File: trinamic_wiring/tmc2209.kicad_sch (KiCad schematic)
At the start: 0 parts

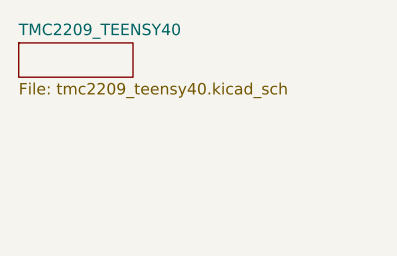
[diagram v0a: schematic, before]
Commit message: Add tmc2209_mega2560
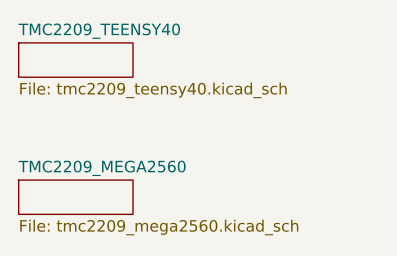
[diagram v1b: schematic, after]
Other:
- added sheet TMC2209_MEGA2560 (tmc2209_mega2560.kicad_sch)
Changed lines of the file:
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@@
+    )
+  )
+  (sheet (at 100.33 50.8) (size 12.7 3.81) (fields_autoplaced)
+    (stroke (width 0.1524) (type solid) (color 0 0 0 0))
+    (fill (color 0 0 0 0.0000))
+    (property "Sheet name" "TMC2209_MEGA2560" (id 0) (at 100.33 50.0884 0)
+      (effects (font (size 1.27 1.27)) (justify left bottom))
+    )
+    (property "Sheet file" "tmc2209_mega2560.kicad_sch" (id 1) (at 100.33 55.1946 0)
+      (effects (font (size 1.27 1.27)) (justify left top))
     )
   )

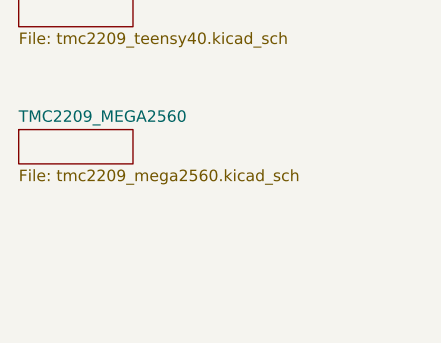
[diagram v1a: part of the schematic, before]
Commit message: Add tmc2209_feather_nrf52
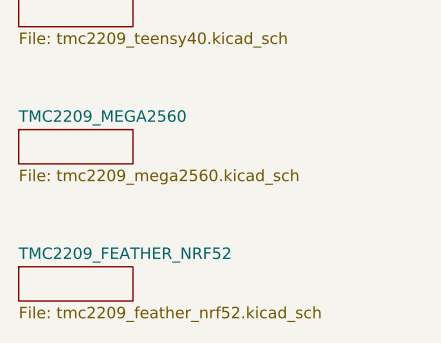
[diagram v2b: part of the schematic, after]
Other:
- added sheet TMC2209_FEATHER_NRF52 (tmc2209_feather_nrf52.kicad_sch)
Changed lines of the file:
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@@
+    )
+  )
+  (sheet (at 100.33 66.04) (size 12.7 3.81) (fields_autoplaced)
+    (stroke (width 0.1524) (type solid) (color 0 0 0 0))
+    (fill (color 0 0 0 0.0000))
+    (property "Sheet name" "TMC2209_FEATHER_NRF52" (id 0) (at 100.33 65.3284 0)
+      (effects (font (size 1.27 1.27)) (justify left bottom))
+    )
+    (property "Sheet file" "tmc2209_feather_nrf52.kicad_sch" (id 1) (at 100.33 70.4346 0)
+      (effects (font (size 1.27 1.27)) (justify left top))
     )
   )

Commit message: Update version
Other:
- company: (none) -> Janelia Research Campus
- title: (none) -> Trinamic Wiring
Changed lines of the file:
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@@
-(kicad_sch (version 20211123) (generator eeschema)
+(kicad_sch (version 20230121) (generator eeschema)
   (paper "A4")
+  (title_block
+    (title "Trinamic Wiring")
+    (date "2023-04-18")
+    (rev "0.3")
+    (company "Janelia Research Campus")
+  )
   (sheet (at 100.33 35.56) (size 12.7 3.81) (fields_autoplaced)
-    (stroke (width 0.1524) (type solid) (color 0 0 0 0))
+    (stroke (width 0.1524) (type solid))
     (fill (color 0 0 0 0.0000))
-    (property "Sheet name" "TMC2209_TEENSY40" (id 0) (at 100.33 34.8484 0)
+    (property "Sheetname" "TMC2209_TEENSY40" (at 100.33 34.8484 0)
       (effects (font (size 1.27 1.27)) (justify left bottom))
     )
-    (property "Sheet file" "tmc2209_teensy40.kicad_sch" (id 1) (at 100.33 39.9546 0)
+    (property "Sheetfile" "tmc2209_teensy40.kicad_sch" (at 100.33 39.9546 0)
       (effects (font (size 1.27 1.27)) (justify left top))
+    )
+    (instances
+      (project "trinamic_wiring"
+        (path "/e4144788-6304-493f-818e-5d881d3b7418/c8eda2b5-ab13-4033-82d9-875c9fcaf884" (page "3"))
+      )
     )
   )
   (sheet (at 100.33 66.04) (size 12.7 3.81) (fields_autoplaced)
-    (stroke (width 0.1524) (type solid) (color 0 0 0 0))
+    (stroke (width 0.1524) (type solid))
     (fill (color 0 0 0 0.0000))
-    (property "Sheet name" "TMC2209_FEATHER_NRF52" (id 0) (at 100.33 65.3284 0)
+    (property "Sheetname" "TMC2209_FEATHER_NRF52" (at 100.33 65.3284 0)
       (effects (font (size 1.27 1.27)) (justify left bottom))
     )
-    (property "Sheet file" "tmc2209_feather_nrf52.kicad_sch" (id 1) (at 100.33 70.4346 0)
+    (property "Sheetfile" "tmc2209_feather_nrf52.kicad_sch" (at 100.33 70.4346 0)
       (effects (font (size 1.27 1.27)) (justify left top))
+    )
+    (instances
+      (project "trinamic_wiring"
+        (path "/e4144788-6304-493f-818e-5d881d3b7418/c8eda2b5-ab13-4033-82d9-875c9fcaf884" (page "5"))
+      )
     )
   )
   (sheet (at 100.33 50.8) (size 12.7 3.81) (fields_autoplaced)
-    (stroke (width 0.1524) (type solid) (color 0 0 0 0))
+    (stroke (width 0.1524) (type solid))
     (fill (color 0 0 0 0.0000))
-    (property "Sheet name" "TMC2209_MEGA2560" (id 0) (at 100.33 50.0884 0)
+    (property "Sheetname" "TMC2209_MEGA2560" (at 100.33 50.0884 0)
       (effects (font (size 1.27 1.27)) (justify left bottom))
     )
-    (property "Sheet file" "tmc2209_mega2560.kicad_sch" (id 1) (at 100.33 55.1946 0)
+    (property "Sheetfile" "tmc2209_mega2560.kicad_sch" (at 100.33 55.1946 0)
       (effects (font (size 1.27 1.27)) (justify left top))
     )
+    (instances
+      (project "trinamic_wiring"
+        (path "/e4144788-6304-493f-818e-5d881d3b7418/c8eda2b5-ab13-4033-82d9-875c9fcaf884" (page "4"))
+      )
+    )
   )

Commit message: Add unidirectional and bidirectional sheets
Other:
- added sheet TMC2209_BIDIRECTIONAL_COUPLED (tmc2209_bidirectional_coupled.kicad_sch)
- added sheet TMC2209_UNIDIRECTIONAL (tmc2209_unidirectional.kicad_sch)
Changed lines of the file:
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@@
     (company "Janelia Research Campus")
+  )
+  (sheet (at 100.33 81.28) (size 12.7 3.81) (fields_autoplaced)
+    (stroke (width 0.1524) (type solid))
+    (fill (color 0 0 0 0.0000))
+    (property "Sheetname" "TMC2209_UNIDIRECTIONAL" (at 100.33 80.5684 0)
+      (effects (font (size 1.27 1.27)) (justify left bottom))
+    )
+    (property "Sheetfile" "tmc2209_unidirectional.kicad_sch" (at 100.33 85.6746 0)
+      (effects (font (size 1.27 1.27)) (justify left top))
+    )
+    (instances
+      (project "trinamic_wiring"
+        (path "/e4144788-6304-493f-818e-5d881d3b7418/c8eda2b5-ab13-4033-82d9-875c9fcaf884" (page "6"))
+      )
+    )
   )
   (sheet (at 100.33 35.56) (size 12.7 3.81) (fields_autoplaced)
@@
       )
     )
+  )
+  (sheet (at 100.33 97.79) (size 12.7 3.81) (fields_autoplaced)
+    (stroke (width 0.1524) (type solid))
+    (fill (color 0 0 0 0.0000))
+    (property "Sheetname" "TMC2209_BIDIRECTIONAL_COUPLED" (at 100.33 97.0784 0)
+      (effects (font (size 1.27 1.27)) (justify left bottom))
+    )
+    (property "Sheetfile" "tmc2209_bidirectional_coupled.kicad_sch" (at 100.33 102.1846 0)
+      (effects (font (size 1.27 1.27)) (justify left top))
+    )
+    (instances
+      (project "trinamic_wiring"
+        (path "/e4144788-6304-493f-818e-5d881d3b7418/c8eda2b5-ab13-4033-82d9-875c9fcaf884" (page "7"))
+      )
+    )

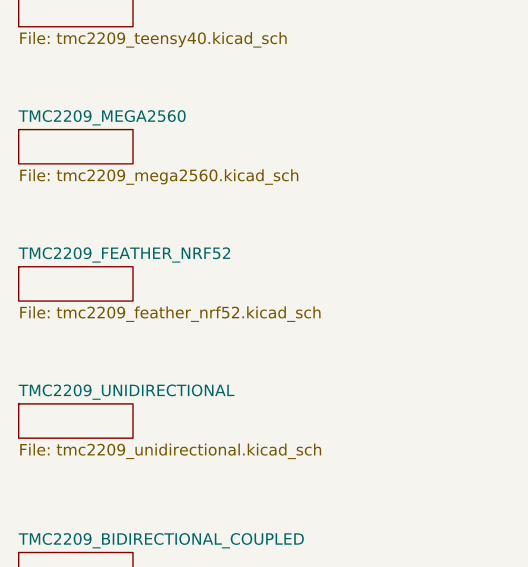
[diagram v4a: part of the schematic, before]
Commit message: Update wiring for TMC2209 v9
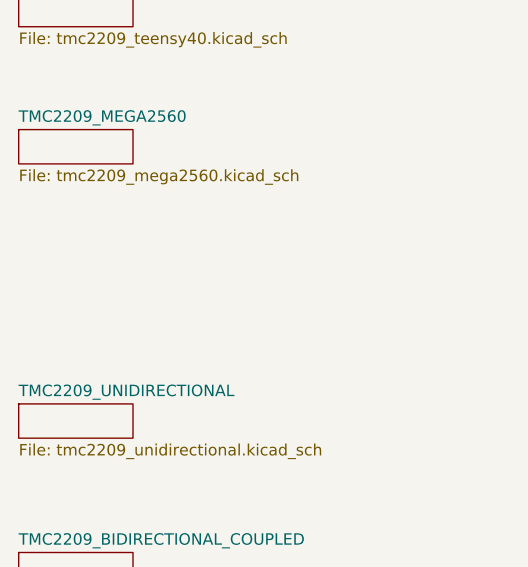
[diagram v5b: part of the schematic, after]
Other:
- removed sheet TMC2209_FEATHER_NRF52
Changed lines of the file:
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@@
   (title_block
     (title "Trinamic Wiring")
-    (date "2023-04-18")
+    (date "2023-04-27")
     (rev "0.3")
     (company "Janelia Research Campus")
@@
       )
     )
-  )
-  (sheet (at 100.33 66.04) (size 12.7 3.81) (fields_autoplaced)
-    (stroke (width 0.1524) (type solid))
-    (fill (color 0 0 0 0.0000))
-    (property "Sheetname" "TMC2209_FEATHER_NRF52" (at 100.33 65.3284 0)
-      (effects (font (size 1.27 1.27)) (justify left bottom))
-    )
-    (property "Sheetfile" "tmc2209_feather_nrf52.kicad_sch" (at 100.33 70.4346 0)
-      (effects (font (size 1.27 1.27)) (justify left top))
-    )
-    (instances
-      (project "trinamic_wiring"
-        (path "/e4144788-6304-493f-818e-5d881d3b7418/c8eda2b5-ab13-4033-82d9-875c9fcaf884" (page "5"))
-      )
-    )

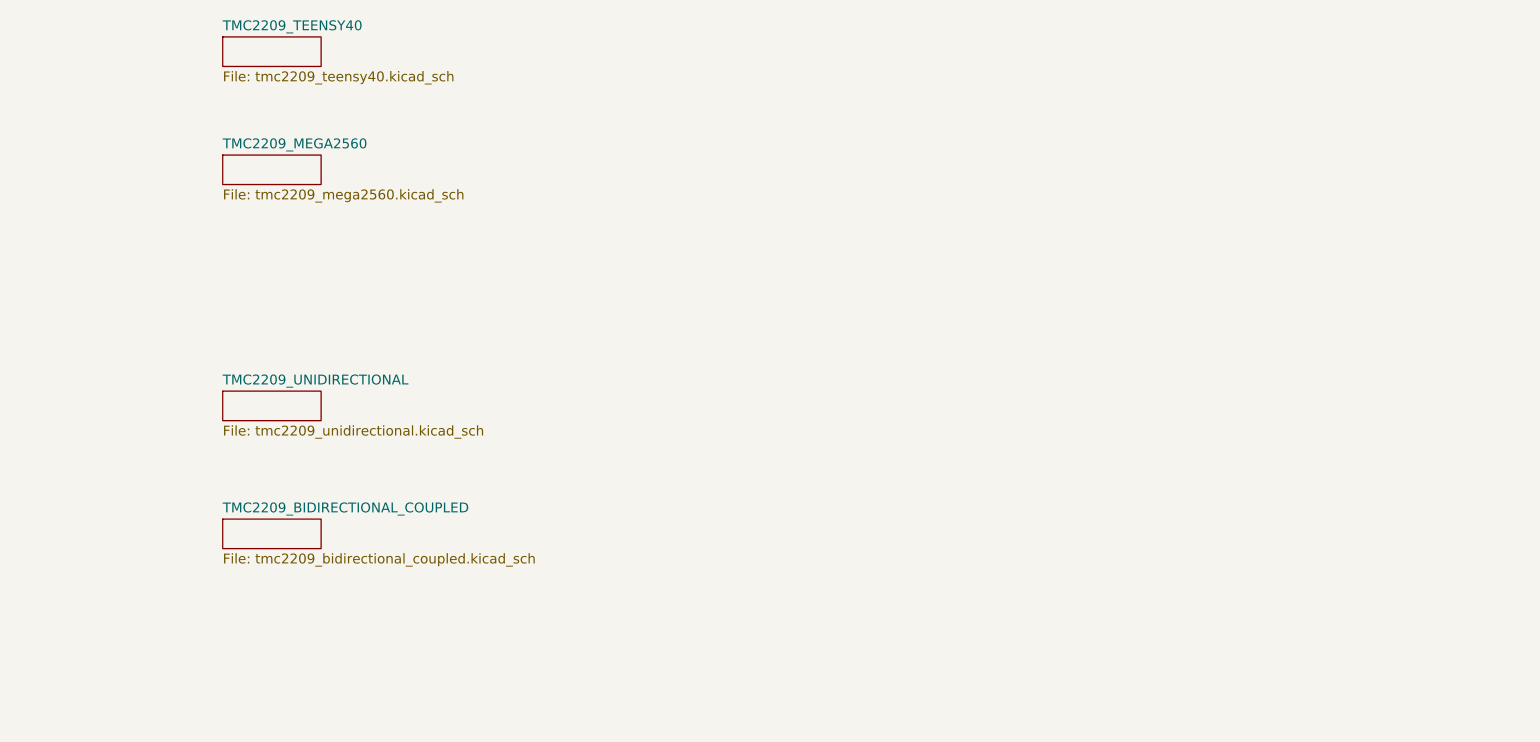
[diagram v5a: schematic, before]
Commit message: Add multiple chip schematics
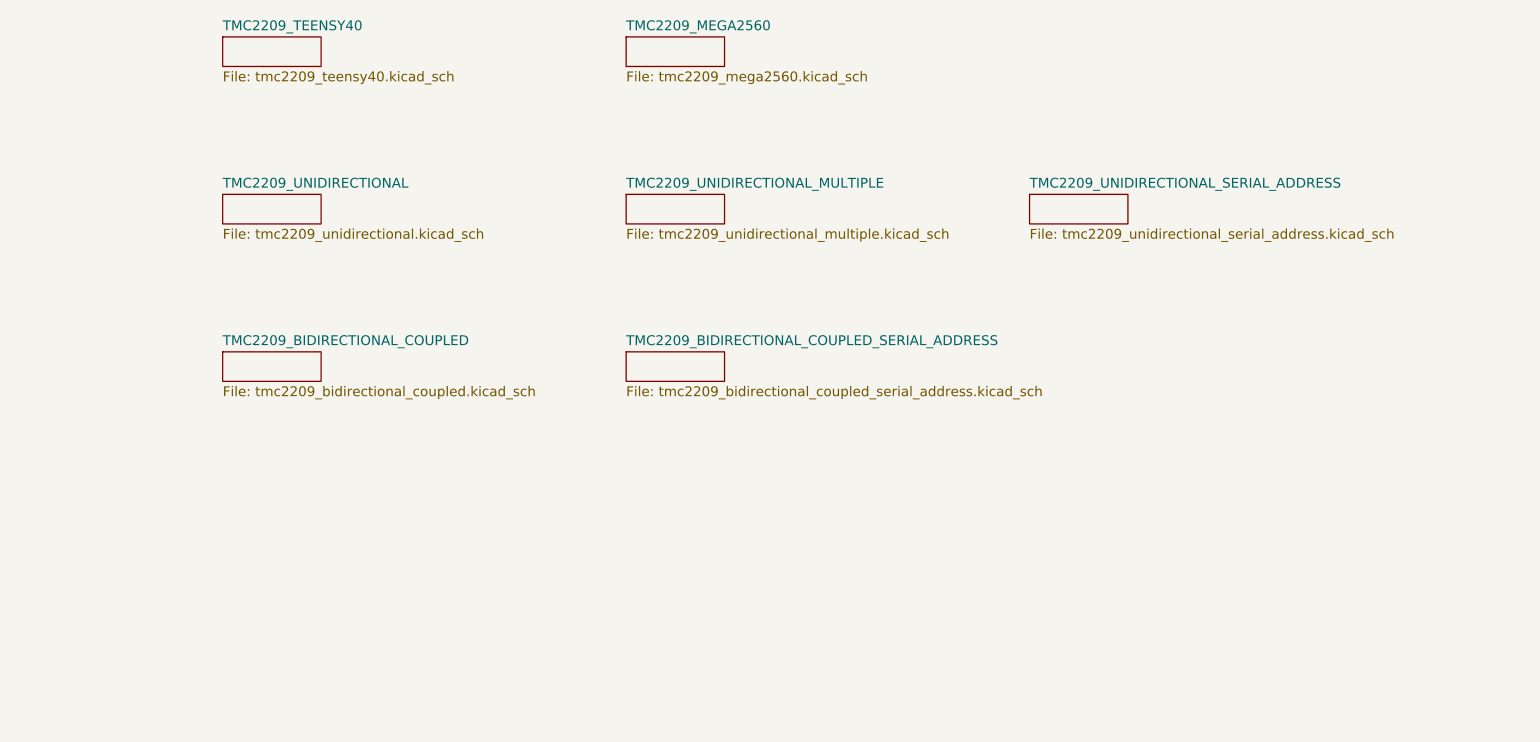
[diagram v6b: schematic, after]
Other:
- added sheet TMC2209_BIDIRECTIONAL_COUPLED_SERIAL_ADDRESS (tmc2209_bidirectional_coupled_serial_address.kicad_sch)
- added sheet TMC2209_UNIDIRECTIONAL_MULTIPLE (tmc2209_unidirectional_multiple.kicad_sch)
- added sheet TMC2209_UNIDIRECTIONAL_SERIAL_ADDRESS (tmc2209_unidirectional_serial_address.kicad_sch)
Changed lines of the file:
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@@
     (company "Janelia Research Campus")
   )
-  (sheet (at 100.33 81.28) (size 12.7 3.81) (fields_autoplaced)
+  (sheet (at 100.33 55.88) (size 12.7 3.81) (fields_autoplaced)
     (stroke (width 0.1524) (type solid))
     (fill (color 0 0 0 0.0000))
-    (property "Sheetname" "TMC2209_UNIDIRECTIONAL" (at 100.33 80.5684 0)
+    (property "Sheetname" "TMC2209_UNIDIRECTIONAL" (at 100.33 55.1684 0)
       (effects (font (size 1.27 1.27)) (justify left bottom))
     )
-    (property "Sheetfile" "tmc2209_unidirectional.kicad_sch" (at 100.33 85.6746 0)
+    (property "Sheetfile" "tmc2209_unidirectional.kicad_sch" (at 100.33 60.2746 0)
       (effects (font (size 1.27 1.27)) (justify left top))
     )
@@
     )
   )
-  (sheet (at 100.33 97.79) (size 12.7 3.81) (fields_autoplaced)
+  (sheet (at 152.4 55.88) (size 12.7 3.81) (fields_autoplaced)
     (stroke (width 0.1524) (type solid))
     (fill (color 0 0 0 0.0000))
-    (property "Sheetname" "TMC2209_BIDIRECTIONAL_COUPLED" (at 100.33 97.0784 0)
+    (property "Sheetname" "TMC2209_UNIDIRECTIONAL_MULTIPLE" (at 152.4 55.1684 0)
       (effects (font (size 1.27 1.27)) (justify left bottom))
     )
-    (property "Sheetfile" "tmc2209_bidirectional_coupled.kicad_sch" (at 100.33 102.1846 0)
+    (property "Sheetfile" "tmc2209_unidirectional_multiple.kicad_sch" (at 152.4 60.2746 0)
+      (effects (font (size 1.27 1.27)) (justify left top))
+    )
+    (instances
+      (project "trinamic_wiring"
+        (path "/e4144788-6304-493f-818e-5d881d3b7418/c8eda2b5-ab13-4033-82d9-875c9fcaf884" (page "8"))
+      )
+    )
+  )
+  (sheet (at 152.4 76.2) (size 12.7 3.81) (fields_autoplaced)
+    (stroke (width 0.1524) (type solid))
+    (fill (color 0 0 0 0.0000))
+    (property "Sheetname" "TMC2209_BIDIRECTIONAL_COUPLED_SERIAL_ADDRESS" (at 152.4 75.4884 0)
+      (effects (font (size 1.27 1.27)) (justify left bottom))
+    )
+    (property "Sheetfile" "tmc2209_bidirectional_coupled_serial_address.kicad_sch" (at 152.4 80.5946 0)
+      (effects (font (size 1.27 1.27)) (justify left top))
+    )
+    (instances
+      (project "trinamic_wiring"
+        (path "/e4144788-6304-493f-818e-5d881d3b7418/c8eda2b5-ab13-4033-82d9-875c9fcaf884" (page "5"))
+      )
+    )
+  )
+  (sheet (at 204.47 55.88) (size 12.7 3.81) (fields_autoplaced)
+    (stroke (width 0.1524) (type solid))
+    (fill (color 0 0 0 0.0000))
+    (property "Sheetname" "TMC2209_UNIDIRECTIONAL_SERIAL_ADDRESS" (at 204.47 55.1684 0)
+      (effects (font (size 1.27 1.27)) (justify left bottom))
+    )
+    (property "Sheetfile" "tmc2209_unidirectional_serial_address.kicad_sch" (at 204.47 60.2746 0)
+      (effects (font (size 1.27 1.27)) (justify left top))
+    )
+    (instances
+      (project "trinamic_wiring"
+        (path "/e4144788-6304-493f-818e-5d881d3b7418/c8eda2b5-ab13-4033-82d9-875c9fcaf884" (page "9"))
+      )
+    )
+  )
+  (sheet (at 100.33 76.2) (size 12.7 3.81) (fields_autoplaced)
+    (stroke (width 0.1524) (type solid))
+    (fill (color 0 0 0 0.0000))
+    (property "Sheetname" "TMC2209_BIDIRECTIONAL_COUPLED" (at 100.33 75.4884 0)
+      (effects (font (size 1.27 1.27)) (justify left bottom))
+    )
+    (property "Sheetfile" "tmc2209_bidirectional_coupled.kicad_sch" (at 100.33 80.5946 0)
       (effects (font (size 1.27 1.27)) (justify left top))
     )
@@
     )
   )
-  (sheet (at 100.33 50.8) (size 12.7 3.81) (fields_autoplaced)
+  (sheet (at 152.4 35.56) (size 12.7 3.81) (fields_autoplaced)
     (stroke (width 0.1524) (type solid))
     (fill (color 0 0 0 0.0000))
-    (property "Sheetname" "TMC2209_MEGA2560" (at 100.33 50.0884 0)
+    (property "Sheetname" "TMC2209_MEGA2560" (at 152.4 34.8484 0)
       (effects (font (size 1.27 1.27)) (justify left bottom))
     )
-    (property "Sheetfile" "tmc2209_mega2560.kicad_sch" (at 100.33 55.1946 0)
+    (property "Sheetfile" "tmc2209_mega2560.kicad_sch" (at 152.4 39.9546 0)
       (effects (font (size 1.27 1.27)) (justify left top))
     )

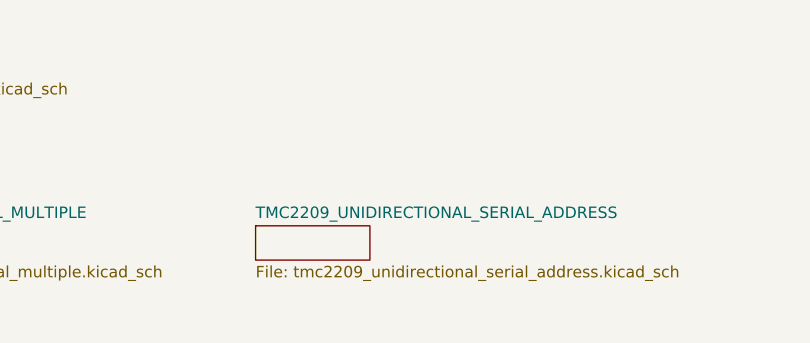
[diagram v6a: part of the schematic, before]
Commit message: Add uno
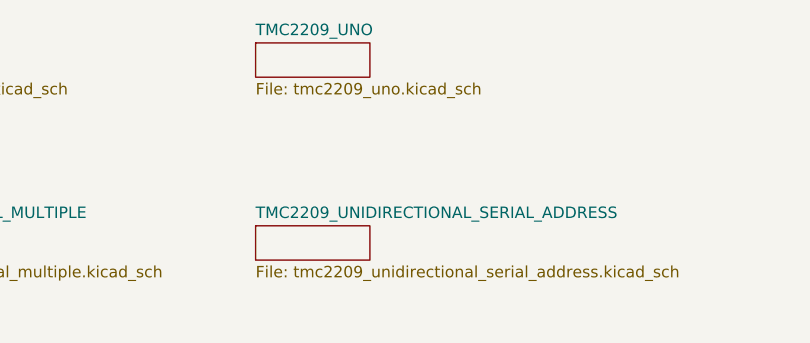
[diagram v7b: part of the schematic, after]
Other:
- added sheet TMC2209_UNO (tmc2209_uno.kicad_sch)
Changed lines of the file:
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@@
   (title_block
     (title "Trinamic Wiring")
-    (date "2023-04-27")
+    (date "2023-06-27")
     (rev "0.3")
     (company "Janelia Research Campus")
@@
       )
     )
+  )
+  (sheet (at 204.47 35.56) (size 12.7 3.81) (fields_autoplaced)
+    (stroke (width 0.1524) (type solid))
+    (fill (color 0 0 0 0.0000))
+    (property "Sheetname" "TMC2209_UNO" (at 204.47 34.8484 0)
+      (effects (font (size 1.27 1.27)) (justify left bottom))
+    )
+    (property "Sheetfile" "tmc2209_uno.kicad_sch" (at 204.47 39.9546 0)
+      (effects (font (size 1.27 1.27)) (justify left top))
+    )
+    (instances
+      (project "trinamic_wiring"
+        (path "/e4144788-6304-493f-818e-5d881d3b7418/c8eda2b5-ab13-4033-82d9-875c9fcaf884" (page "10"))
+      )
+    )
